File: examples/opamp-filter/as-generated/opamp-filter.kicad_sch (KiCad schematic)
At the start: 27 parts, among them J1 IN, J2 5V, J3 OUT, U1 MCP6001R, U2 MCP6001R

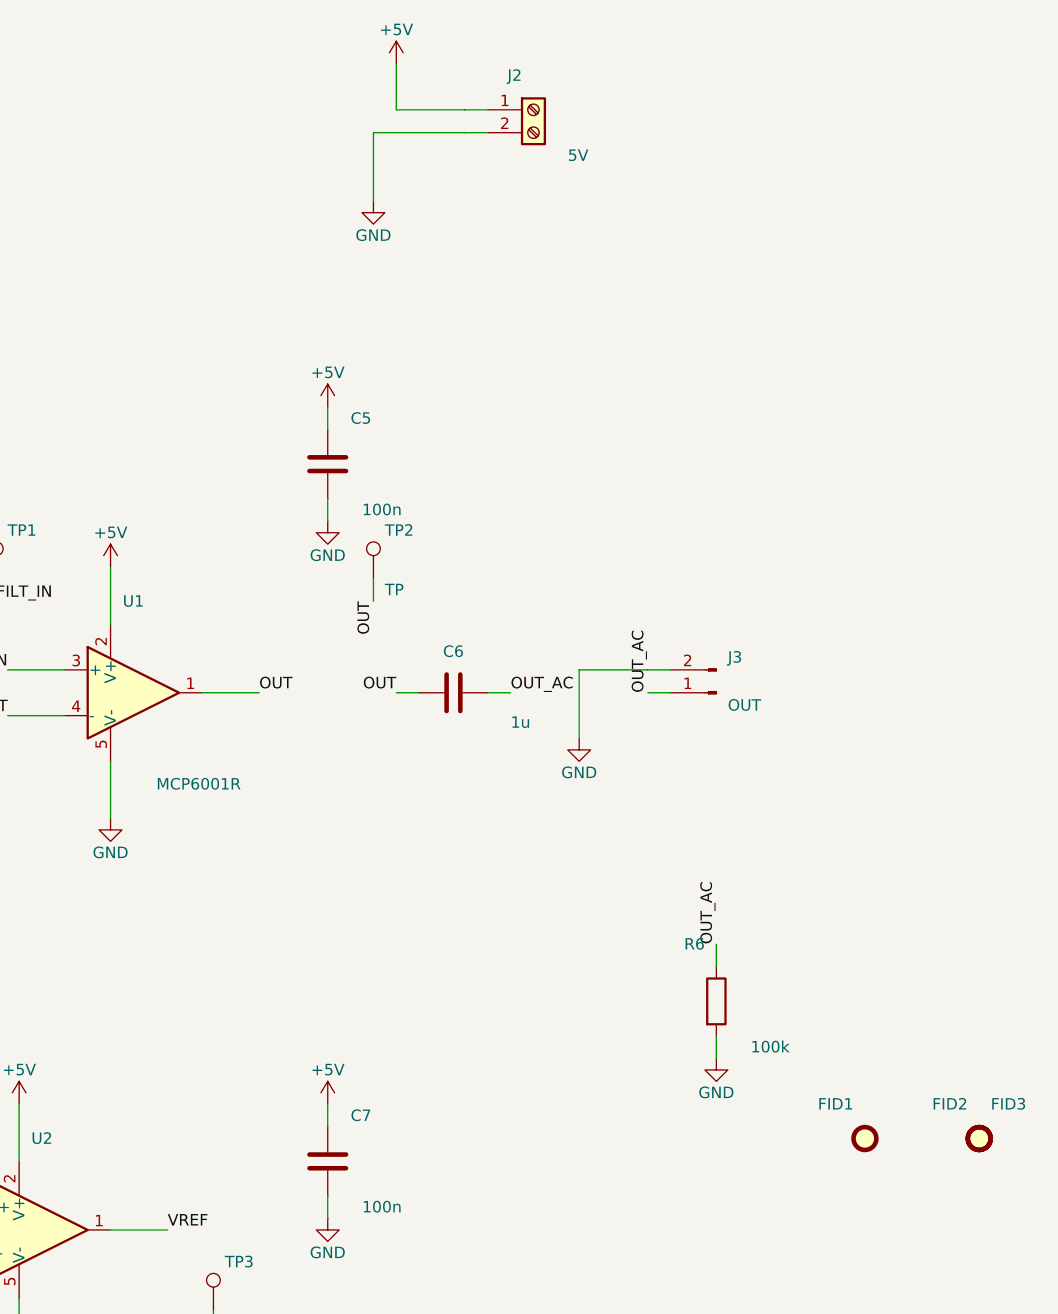
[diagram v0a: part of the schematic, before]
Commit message: chore(examples): regenerate the four two-layer boards and their pictures
buck-5v, motor-driver, pico-carrier and opamp-filter, regenerated from the
merged generator and gated clean on KiCad 9.0.9. The inner-layer pictures go
with the inner layers.

fpga-audio is still routing; it follows.

Co-Authored-By: Claude Opus 5 <noreply@anthropic.com>
Claude-Session: https://claude.ai/code/session_01XQE7UkE9WTSMW3oZ3kLeCt
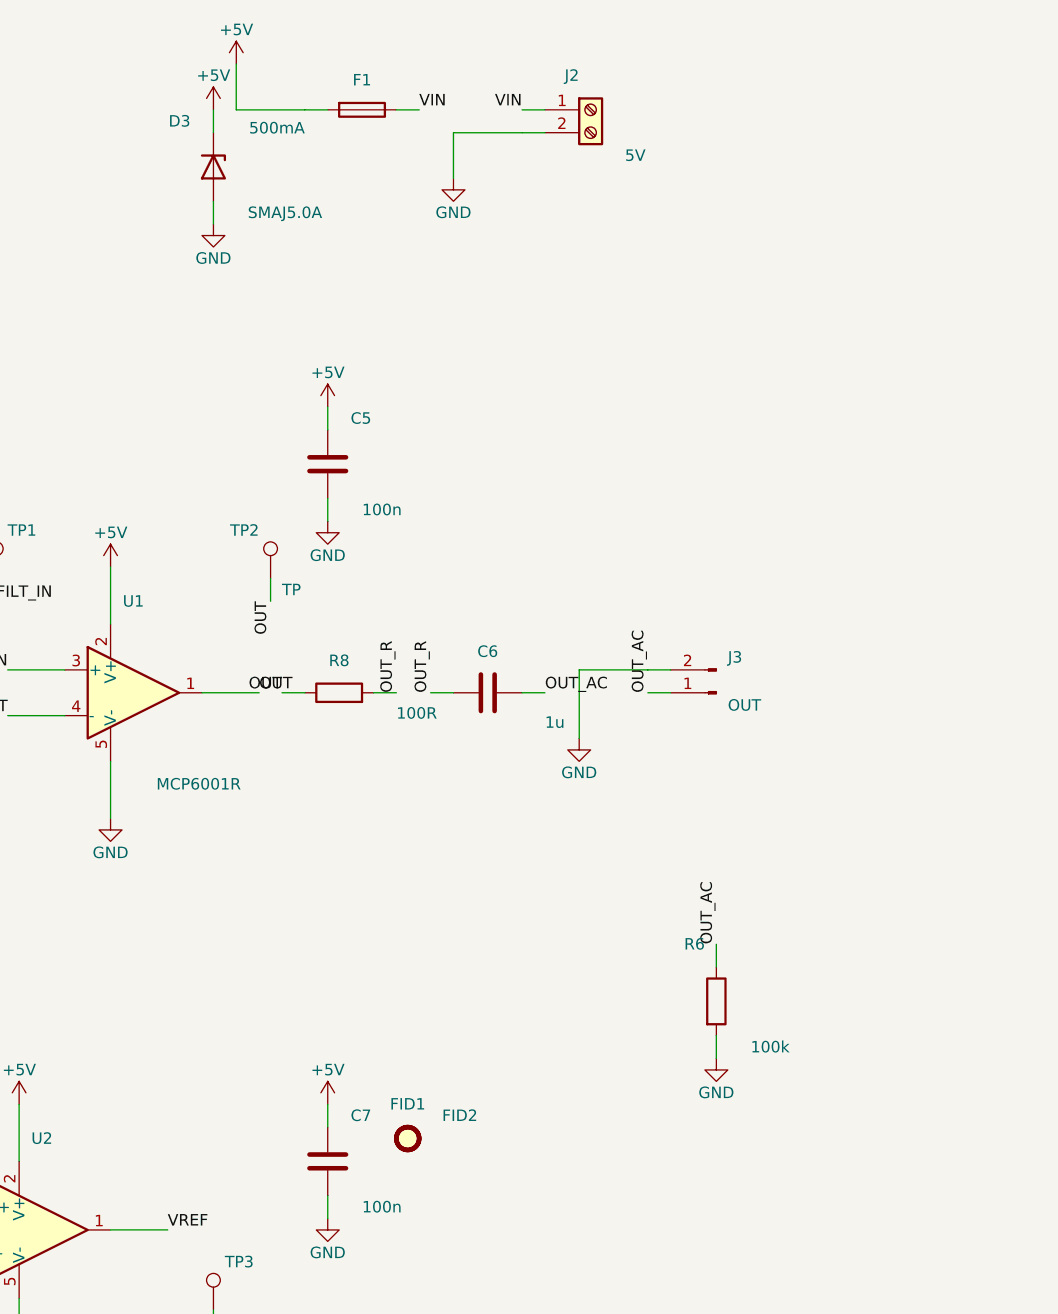
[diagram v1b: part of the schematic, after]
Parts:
- removed FID3: Fiducial, Fiducial:Fiducial_1mm_Mask2mm, symbol Mechanical:Fiducial
- added D3: SMAJ5.0A, Diode_SMD:D_SMA, symbol Device:D_Zener
- added F1: 500mA, Fuse:Fuse_1206_3216Metric, symbol Device:Fuse
- added R8: 100R, Resistor_SMD:R_0805_2012Metric, symbol Device:R
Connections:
- net +5V: now also D3.1 (K), F1.2; no longer J2.1 (Pin_1)
- net GND: now also D3.2 (A)
- net OUT: now also R8.1; no longer C6.1
- new net OUT_R: C6.1, R8.2
- new net VIN: F1.1, J2.1 (Pin_1)
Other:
- moved on the sheet: C6, FID1, FID2, J2, TP2
